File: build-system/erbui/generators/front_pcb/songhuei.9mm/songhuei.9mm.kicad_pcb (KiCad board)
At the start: 2 copper layers, 1 part

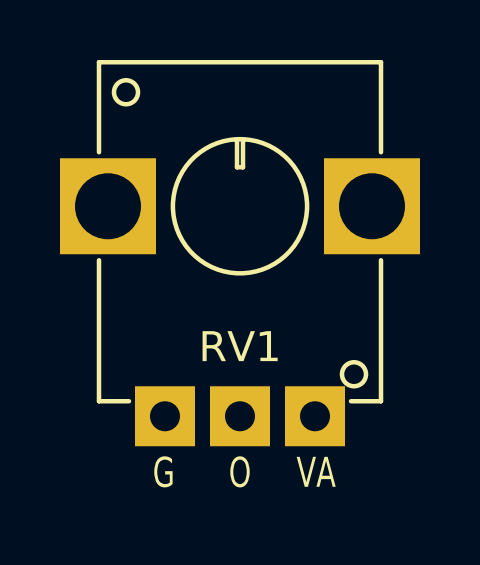
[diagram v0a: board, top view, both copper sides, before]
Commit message: Update erbui front pcb generator blocks labels to match boards conventions
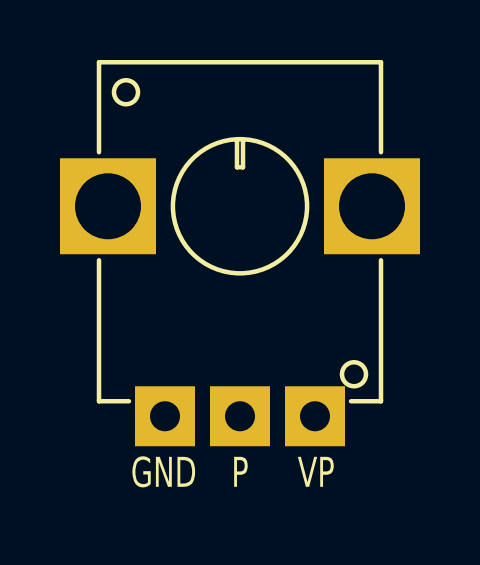
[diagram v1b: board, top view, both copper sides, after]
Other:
- board text added: "GND"
- board text added: "P"
- board text added: "VP"
- board text removed: "G"
- board text removed: "O"
- board text removed: "VA"
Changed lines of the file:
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@@
   (module Potentiometer_Thonk:SongHueiTallTrim9 (layer F.Cu)
     (at 0 0)
-    (fp_text reference RV1 (at 0 4.7) (layer F.SilkS)
+    (fp_text reference RV1 (at 0 4.7) (layer F.SilkS) hide
       (effects (font (size 1 1) (thickness 0.15)))
     )
@@
       (effects (font (size 1 1) (thickness 0.15)))
     )
+    (fp_line (start -0.1 -2.2) (end -0.1 -1.3) (layer F.SilkS) (width 0.15))
+    (fp_line (start -0.1 -1.3) (end 0.1 -1.3) (layer F.SilkS) (width 0.15))
+    (fp_line (start 0.1 -1.3) (end 0.1 -2.2) (layer F.SilkS) (width 0.15))
+    (fp_circle (center 0 0) (end 2.2 0.4) (layer F.SilkS) (width 0.15))
+    (fp_circle (center 3.8 5.6) (end 4.2 5.6) (layer F.SilkS) (width 0.15))
+    (fp_circle (center -3.8 -3.8) (end -4.2 -3.8) (layer F.SilkS) (width 0.15))
+    (fp_line (start 3.7 6.5) (end 4.7 6.5) (layer F.SilkS) (width 0.15))
+    (fp_line (start 4.7 1.8) (end 4.7 6.5) (layer F.SilkS) (width 0.15))
+    (fp_line (start -4.7 1.8) (end -4.7 6.5) (layer F.SilkS) (width 0.15))
+    (fp_line (start -4.7 6.5) (end -3.7 6.5) (layer F.SilkS) (width 0.15))
+    (fp_line (start -4.7 -4.8) (end -4.7 -1.8) (layer F.SilkS) (width 0.15))
+    (fp_line (start 4.7 -4.8) (end 4.7 -1.8) (layer F.SilkS) (width 0.15))
     (fp_line (start -4.7 -4.8) (end 4.7 -4.8) (layer F.SilkS) (width 0.15))
-    (fp_line (start 4.7 -4.8) (end 4.7 -1.8) (layer F.SilkS) (width 0.15))
-    (fp_line (start -4.7 -4.8) (end -4.7 -1.8) (layer F.SilkS) (width 0.15))
-    (fp_line (start -4.7 6.5) (end -3.7 6.5) (layer F.SilkS) (width 0.15))
-    (fp_line (start -4.7 1.8) (end -4.7 6.5) (layer F.SilkS) (width 0.15))
-    (fp_line (start 4.7 1.8) (end 4.7 6.5) (layer F.SilkS) (width 0.15))
-    (fp_line (start 3.7 6.5) (end 4.7 6.5) (layer F.SilkS) (width 0.15))
-    (fp_circle (center -3.8 -3.8) (end -4.2 -3.8) (layer F.SilkS) (width 0.15))
-    (fp_circle (center 3.8 5.6) (end 4.2 5.6) (layer F.SilkS) (width 0.15))
-    (fp_circle (center 0 0) (end 2.2 0.4) (layer F.SilkS) (width 0.15))
-    (fp_line (start 0.1 -1.3) (end 0.1 -2.2) (layer F.SilkS) (width 0.15))
-    (fp_line (start -0.1 -1.3) (end 0.1 -1.3) (layer F.SilkS) (width 0.15))
-    (fp_line (start -0.1 -2.2) (end -0.1 -1.3) (layer F.SilkS) (width 0.15))
     (pad "" thru_hole rect (at 4.4 0) (size 3.2 3.2) (drill 2.2) (layers *.Cu *.Mask))
     (pad 3 thru_hole rect (at 2.5 7) (size 2 2) (drill 1) (layers *.Cu *.Mask)
@@
     (pad "" thru_hole rect (at -4.4 0) (size 3.2 3.2) (drill 2.2) (layers *.Cu *.Mask))
   )
-  (gr_text VA (at 2.54 8.89) (layer F.SilkS)
+  (gr_text VP (at 2.54 8.89) (layer F.SilkS)
     (effects (font (size 1 0.7) (thickness 0.15)))
   )
-  (gr_text O (at 0 8.89) (layer F.SilkS)
+  (gr_text P (at 0 8.89) (layer F.SilkS)
     (effects (font (size 1 0.7) (thickness 0.15)))
   )
-  (gr_text G (at -2.54 8.89) (layer F.SilkS)
+  (gr_text GND (at -2.54 8.89) (layer F.SilkS)
     (effects (font (size 1 0.7) (thickness 0.15)))
   )

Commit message: Use pads to ease soldering
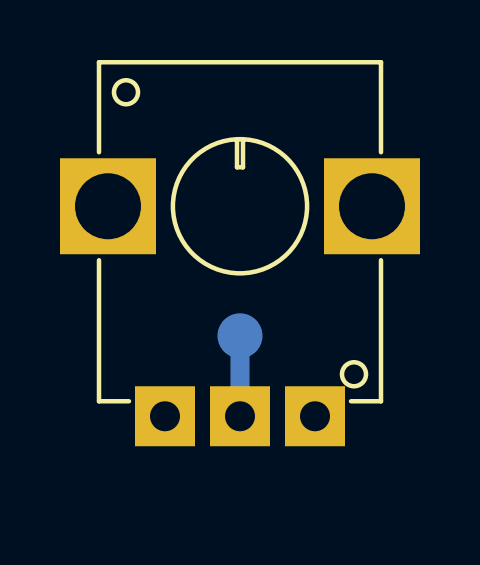
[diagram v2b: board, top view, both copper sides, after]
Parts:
- added O1: TestPoint, TestPoint:TestPoint_Pad_D1.5mm, B.Cu at (0.00, 4.32)
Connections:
- net Net-(RV1-Pad1) renamed GND
- net Net-(RV1-Pad3) renamed +3V3
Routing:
- net Net-(O1-Pad1): track 0.00 -> 2.68 mm
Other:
- board text added: "O"
- board text removed: "GND"
- board text removed: "P"
- board text removed: "VP"
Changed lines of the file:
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@@
   (general
     (thickness 1.6)
-    (drawings 3)
-    (tracks 0)
+    (drawings 1)
+    (tracks 1)
     (zones 0)
-    (modules 1)
+    (modules 2)
     (nets 4)
   )
@@
   )
   (net 0 "")
-  (net 1 "Net-(RV1-Pad3)")
-  (net 2 "Net-(RV1-Pad2)")
-  (net 3 "Net-(RV1-Pad1)")
+  (net 1 "Net-(O1-Pad1)")
+  (net 2 +3V3)
+  (net 3 GND)
   (net_class Default "This is the default net class."
     (clearance 0.1524)
@@
     (diff_pair_width 0.1524)
     (diff_pair_gap 0.1524)
-    (add_net "Net-(RV1-Pad1)")
-    (add_net "Net-(RV1-Pad2)")
-    (add_net "Net-(RV1-Pad3)")
+    (add_net +3V3)
+    (add_net GND)
+    (add_net "Net-(O1-Pad1)")
   )
   (module Potentiometer_Thonk:SongHueiTallTrim9 (layer F.Cu)
@@
     (pad "" thru_hole rect (at 4.4 0) (size 3.2 3.2) (drill 2.2) (layers *.Cu *.Mask))
     (pad 3 thru_hole rect (at 2.5 7) (size 2 2) (drill 1) (layers *.Cu *.Mask)
-      (net 1 "Net-(RV1-Pad3)"))
+      (net 2 +3V3))
     (pad 2 thru_hole rect (at 0 7) (size 2 2) (drill 1) (layers *.Cu *.Mask)
-      (net 2 "Net-(RV1-Pad2)"))
+      (net 1 "Net-(O1-Pad1)"))
     (pad 1 thru_hole rect (at -2.5 7) (size 2 2) (drill 1) (layers *.Cu *.Mask)
-      (net 3 "Net-(RV1-Pad1)"))
+      (net 3 GND))
     (pad "" thru_hole rect (at -4.4 0) (size 3.2 3.2) (drill 2.2) (layers *.Cu *.Mask))
   )
-  (gr_text VP (at 2.54 8.89) (layer F.SilkS)
-    (effects (font (size 1 0.7) (thickness 0.15)))
+  (module TestPoint:TestPoint_Pad_D1.5mm (layer B.Cu)
+    (at 0 4.318)
+    (descr "SMD pad as test Point, diameter 1.5mm")
+    (tags "test point SMD pad")
+    (attr virtual)
+    (fp_text reference O1 (at 0 1.648) (layer B.SilkS) hide
+      (effects (font (size 1 1) (thickness 0.15)) (justify mirror))
+    )
+    (fp_text value TestPoint (at 0 -1.75) (layer B.Fab)
+      (effects (font (size 1 1) (thickness 0.15)) (justify mirror))
+    )
+    (fp_circle (center 0 0) (end 1.25 0) (layer B.CrtYd) (width 0.05))
+    (fp_circle (center 0 0) (end 0 -0.95) (layer B.SilkS) (width 0.12))
+    (fp_text user %R (at 0 1.65) (layer B.Fab)
+      (effects (font (size 1 1) (thickness 0.15)) (justify mirror))
+    )
+    (pad 1 smd circle (at 0 0) (size 1.5 1.5) (layers B.Cu B.Mask)
+      (net 1 "Net-(O1-Pad1)"))
   )
-  (gr_text P (at 0 8.89) (layer F.SilkS)
-    (effects (font (size 1 0.7) (thickness 0.15)))
+  (gr_text O (at 1.651 4.318) (layer B.SilkS)
+    (effects (font (size 1 1) (thickness 0.15)) (justify mirror))
   )
-  (gr_text GND (at -2.54 8.89) (layer F.SilkS)
-    (effects (font (size 1 0.7) (thickness 0.15)))
-  )
+  (segment (start 0 7) (end 0 4.318) (width 0.635) (layer B.Cu) (net 1))
 )

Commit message: Generate pin associations
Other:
- board text added: "pin"
- board text removed: "O"
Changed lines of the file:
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@@
       (effects (font (size 1 1) (thickness 0.15)))
     )
+    (fp_line (start -4.7 -4.8) (end 4.7 -4.8) (layer F.SilkS) (width 0.15))
+    (fp_line (start 4.7 -4.8) (end 4.7 -1.8) (layer F.SilkS) (width 0.15))
+    (fp_line (start -4.7 -4.8) (end -4.7 -1.8) (layer F.SilkS) (width 0.15))
+    (fp_line (start -4.7 6.5) (end -3.7 6.5) (layer F.SilkS) (width 0.15))
+    (fp_line (start -4.7 1.8) (end -4.7 6.5) (layer F.SilkS) (width 0.15))
+    (fp_line (start 4.7 1.8) (end 4.7 6.5) (layer F.SilkS) (width 0.15))
+    (fp_line (start 3.7 6.5) (end 4.7 6.5) (layer F.SilkS) (width 0.15))
+    (fp_circle (center -3.8 -3.8) (end -4.2 -3.8) (layer F.SilkS) (width 0.15))
+    (fp_circle (center 3.8 5.6) (end 4.2 5.6) (layer F.SilkS) (width 0.15))
+    (fp_circle (center 0 0) (end 2.2 0.4) (layer F.SilkS) (width 0.15))
+    (fp_line (start 0.1 -1.3) (end 0.1 -2.2) (layer F.SilkS) (width 0.15))
+    (fp_line (start -0.1 -1.3) (end 0.1 -1.3) (layer F.SilkS) (width 0.15))
     (fp_line (start -0.1 -2.2) (end -0.1 -1.3) (layer F.SilkS) (width 0.15))
-    (fp_line (start -0.1 -1.3) (end 0.1 -1.3) (layer F.SilkS) (width 0.15))
-    (fp_line (start 0.1 -1.3) (end 0.1 -2.2) (layer F.SilkS) (width 0.15))
-    (fp_circle (center 0 0) (end 2.2 0.4) (layer F.SilkS) (width 0.15))
-    (fp_circle (center 3.8 5.6) (end 4.2 5.6) (layer F.SilkS) (width 0.15))
-    (fp_circle (center -3.8 -3.8) (end -4.2 -3.8) (layer F.SilkS) (width 0.15))
-    (fp_line (start 3.7 6.5) (end 4.7 6.5) (layer F.SilkS) (width 0.15))
-    (fp_line (start 4.7 1.8) (end 4.7 6.5) (layer F.SilkS) (width 0.15))
-    (fp_line (start -4.7 1.8) (end -4.7 6.5) (layer F.SilkS) (width 0.15))
-    (fp_line (start -4.7 6.5) (end -3.7 6.5) (layer F.SilkS) (width 0.15))
-    (fp_line (start -4.7 -4.8) (end -4.7 -1.8) (layer F.SilkS) (width 0.15))
-    (fp_line (start 4.7 -4.8) (end 4.7 -1.8) (layer F.SilkS) (width 0.15))
-    (fp_line (start -4.7 -4.8) (end 4.7 -4.8) (layer F.SilkS) (width 0.15))
     (pad "" thru_hole rect (at 4.4 0) (size 3.2 3.2) (drill 2.2) (layers *.Cu *.Mask))
     (pad 3 thru_hole rect (at 2.5 7) (size 2 2) (drill 1) (layers *.Cu *.Mask)
@@
       (effects (font (size 1 1) (thickness 0.15)) (justify mirror))
     )
+    (fp_circle (center 0 0) (end 0 -0.95) (layer B.SilkS) (width 0.12))
     (fp_circle (center 0 0) (end 1.25 0) (layer B.CrtYd) (width 0.05))
-    (fp_circle (center 0 0) (end 0 -0.95) (layer B.SilkS) (width 0.12))
     (fp_text user %R (at 0 1.65) (layer B.Fab)
       (effects (font (size 1 1) (thickness 0.15)) (justify mirror))
@@
       (net 1 "Net-(O1-Pad1)"))
   )
-  (gr_text O (at 1.651 4.318) (layer B.SilkS)
-    (effects (font (size 1 1) (thickness 0.15)) (justify mirror))
+  (gr_text pin (at 0.95 4.318) (layer B.SilkS)
+    (effects (font (size 1 1) (thickness 0.15)) (justify right mirror))
   )
   (segment (start 0 7) (end 0 4.318) (width 0.635) (layer B.Cu) (net 1))
